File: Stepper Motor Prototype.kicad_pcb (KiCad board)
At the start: 2 copper layers, 37 parts, among them J1 USB_B_Micro, J2 Screw_Terminal_01x02, J3 Screw_Terminal_01x04, Q1 STD20NF06L, Q2 STD20NF06L, Q3 STD20NF06L, Q4 STD20NF06L, Q5 STD20NF06L, Q6 STD20NF06L, Q7 STD20NF06L, Q8 STD20NF06L, U1 FT232RL, U2 ESP8266EX, U3 LM2595SX-3.3_NOPB, U4 MSP430G2553IPW28, U5 LM2595SX-5.0_NOPB, U6 S25FL512SAGMFIG11, U7 DRV8711

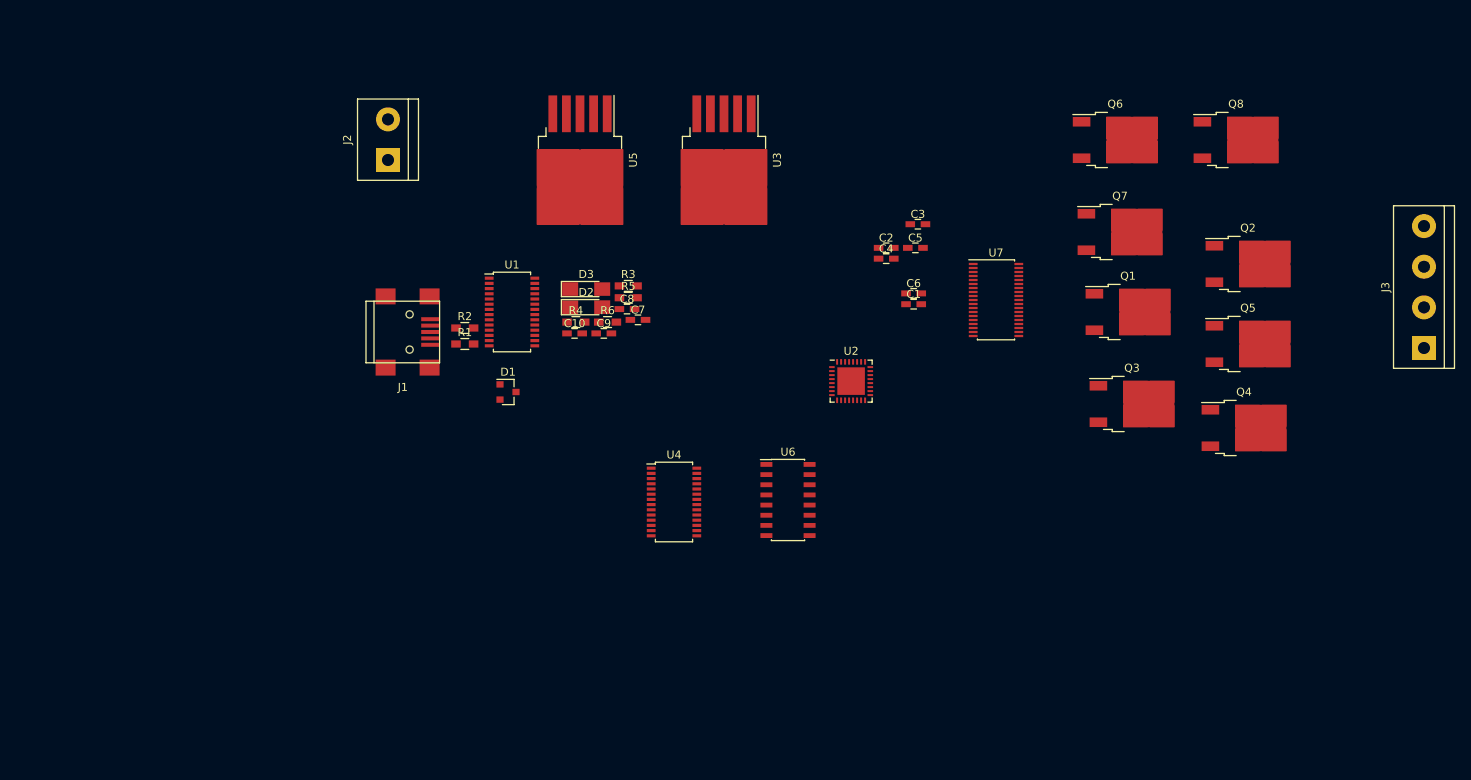
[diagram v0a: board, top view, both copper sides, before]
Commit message: committing before ripping whole board up.  Board will now only contain power seciton and 1 stepper driver
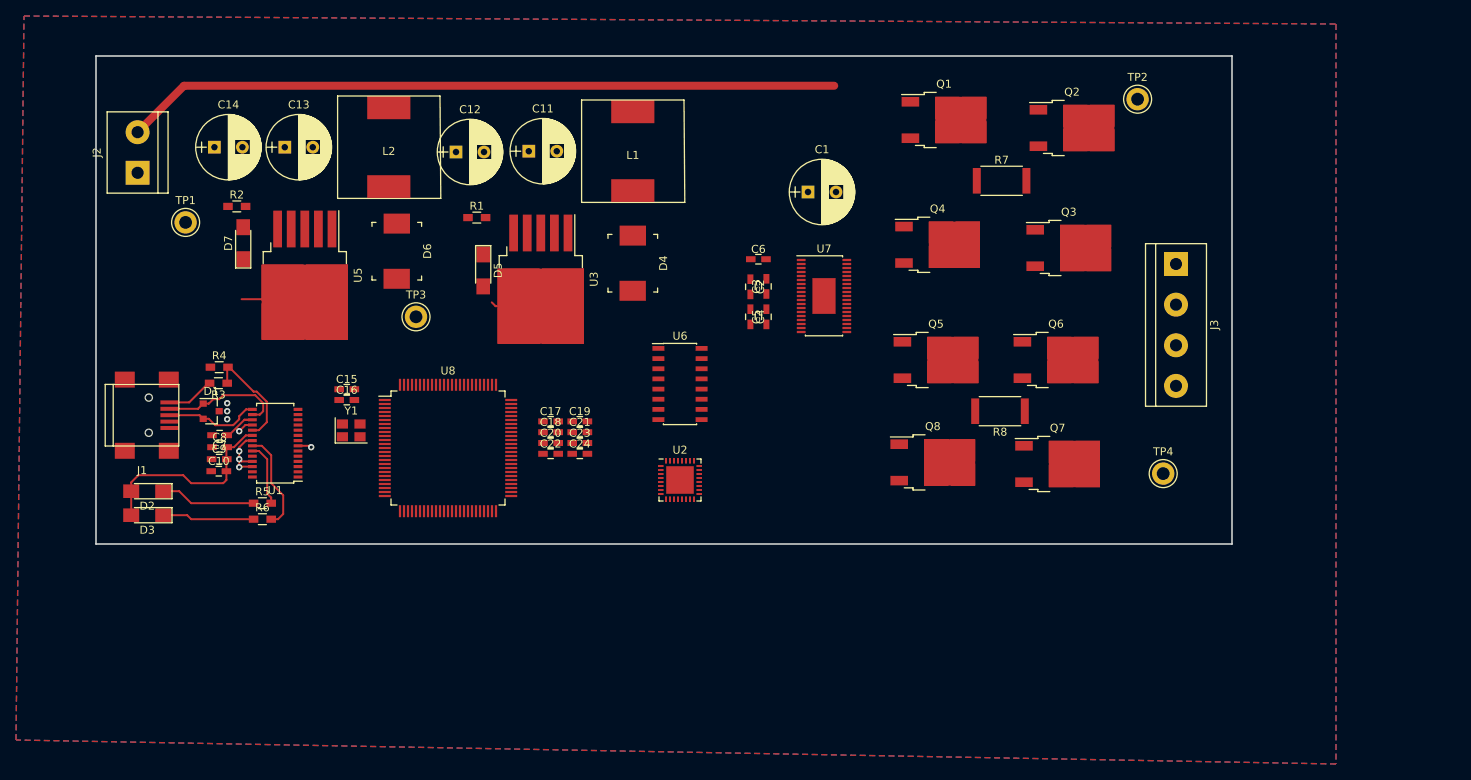
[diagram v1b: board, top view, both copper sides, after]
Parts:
- removed U4: MSP430G2553IPW28, Housings_SSOP:TSSOP-28_4.4x9.7mm_Pitch0.65mm
- added C11: 120uF, Capacitors_THT:CP_Radial_D8.0mm_P3.50mm, F.Cu at (124.1, 68.9)
- added C12: 150uF, Capacitors_THT:CP_Radial_D8.0mm_P3.50mm, F.Cu at (115.0, 69.0)
- added C13: 120uF, Capacitors_THT:CP_Radial_D8.0mm_P3.50mm, F.Cu at (93.6, 68.4)
- added C14: 150uF, Capacitors_THT:CP_Radial_D8.0mm_P3.50mm, F.Cu at (84.8, 68.4)
- added C15: C, Capacitors_SMD:C_0603_HandSoldering, F.Cu at (101.3, 98.7)
- added C16: C, Capacitors_SMD:C_0603_HandSoldering, F.Cu at (101.3, 100.0)
- added C17: 0.1uF, Capacitors_SMD:C_0603_HandSoldering, F.Cu at (126.8, 102.7)
- added C18: 0.1uF, Capacitors_SMD:C_0603_HandSoldering, F.Cu at (126.8, 104.0)
- added C19: 0.1uF, Capacitors_SMD:C_0603_HandSoldering, F.Cu at (130.5, 102.7)
- added C20: 0.1uF, Capacitors_SMD:C_0603_HandSoldering, F.Cu at (126.8, 105.4)
- added C21: 0.1uF, Capacitors_SMD:C_0603_HandSoldering, F.Cu at (130.5, 104.0)
- added C22: 0.1uF, Capacitors_SMD:C_0603_HandSoldering, F.Cu at (126.8, 106.7)
- added C23: 0.1uF, Capacitors_SMD:C_0603_HandSoldering, F.Cu at (130.5, 105.4)
- added C24: 0.1uF, Capacitors_SMD:C_0603_HandSoldering, F.Cu at (130.5, 106.7)
- added D4: D_Schottky, digikey-footprints:DO-214AB, F.Cu at (137.1, 82.9)
- added D5: LED, LEDs:LED_1206_HandSoldering, F.Cu at (118.4, 83.8)
- added D6: D_Schottky, digikey-footprints:DO-214AB, F.Cu at (107.6, 81.4)
- added D7: LED, LEDs:LED_1206_HandSoldering, F.Cu at (88.4, 80.4)
- added L1: 100uH, my_inductors:Wurth_SMD_Inductor_7447709101, F.Cu at (137.1, 68.9)
- added L2: L, my_inductors:Wurth_SMD_Inductor_7447709101, F.Cu at (106.6, 68.4)
- added R7: 0.05R, Resistors_SMD:R_2512, F.Cu at (183.2, 72.6)
- added R8: 0.05R, Resistors_SMD:R_2512, F.Cu at (183.0, 101.4)
- added TP1: TestPoint, Measurement_Points:Test_Point_Keystone_5010-5014_Multipurpose, F.Cu at (81.2, 77.8)
- added TP2: TestPoint, Measurement_Points:Test_Point_Keystone_5010-5014_Multipurpose, F.Cu at (200.2, 62.4)
- added TP3: TestPoint, Measurement_Points:Test_Point_Keystone_5010-5014_Multipurpose, F.Cu at (110.0, 89.6)
- added TP4: TestPoint, Measurement_Points:Test_Point_Keystone_5010-5014_Multipurpose, F.Cu at (203.4, 109.2)
- added U8: STM32F407VGTx, Housings_QFP:LQFP-100_14x14mm_Pitch0.5mm, F.Cu at (114.0, 106.0)
- added Y1: Crystal_GND24, Crystals:Crystal_SMD_SeikoEpson_TSX3225-4pin_3.2x2.5mm, F.Cu at (101.9, 103.8)
- C1: footprint Capacitors_SMD:C_0603_HandSoldering -> Capacitors_THT:CP_Radial_D8.0mm_P3.50mm
- D2: value LED -> TX_LED
- D3: value LED -> RX_LED
- R1, R2: value 68R -> 330R
- U7: footprint Housings_SSOP:TSSOP-38_4.4x9.7mm_Pitch0.5mm -> rca_switch_through_hole:TSSOP-38-1_PowerPad_4.4x9.7mm_Pitch0.5mm
- moved D3 61.7 mm to (76.4, 114.4), turned to 180 degrees
- moved D2 59.5 mm to (76.4, 111.4), turned to 180 degrees
- moved Q8 55.3 mm to (174.6, 107.8)
- moved C7 54.2 mm to (85.5, 104.4), turned to 180 degrees
- moved C8 53.8 mm to (85.5, 105.9)
- moved R3 52.7 mm to (85.3, 97.9), turned to 180 degrees
- moved R5 52.5 mm to (90.8, 112.9)
- moved C9 50.6 mm to (85.4, 107.4)
- moved R6 49.7 mm to (90.8, 114.9)
- moved C10 47.7 mm to (85.3, 108.9)
- moved R4 44.9 mm to (85.4, 95.9)
- moved Q4 44.6 mm to (175.2, 80.6)
- moved Q5 39.1 mm to (175.0, 95.0)
- moved U5 37.3 mm to (96.1, 84.4)
- moved D1 37.2 mm to (84.4, 101.4)
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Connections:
- J1 pad 4: Net-(J1-Pad4) -> (no net)
- Q1 pad 2: Net-(Q1-Pad2) -> +24V
- Q1 pad 3: Net-(Q1-Pad3) -> Net-(J3-Pad1)
- Q2 pad 2: Net-(Q2-Pad2) -> Net-(J3-Pad1)
- Q3 pad 2: Net-(Q3-Pad2) -> Net-(J3-Pad2)
- Q3 pad 3: Net-(Q3-Pad3) -> Net-(Q2-Pad3)
- Q4 pad 2: Net-(Q4-Pad2) -> +24V
- Q4 pad 3: Net-(Q4-Pad3) -> Net-(J3-Pad2)
- Q5 pad 2: Net-(Q5-Pad2) -> +24V
- Q5 pad 3: Net-(Q5-Pad3) -> Net-(J3-Pad3)
- Q6 pad 2: Net-(Q6-Pad2) -> Net-(J3-Pad3)
- Q6 pad 3: Net-(Q6-Pad3) -> Net-(J3-Pad4)
- Q7 pad 3: Net-(Q7-Pad3) -> Net-(J3-Pad4)
- Q8 pad 2: Net-(Q8-Pad2) -> +24V
- Q8 pad 3: Net-(Q8-Pad3) -> Net-(Q7-Pad2)
- R1 pad 1: Net-(R1-Pad1) -> Net-(D5-Pad2)
- R1 pad 2: Net-(D1-Pad2) -> +3V3
- R2 pad 1: Net-(R2-Pad1) -> Net-(D7-Pad2)
- R2 pad 2: Net-(D1-Pad1) -> +5V
- U1 pad 1: Net-(U1-Pad1) -> (no net)
- U1 pad 10: Net-(U1-Pad10) -> (no net)
- U1 pad 11: Net-(U1-Pad11) -> (no net)
- U1 pad 12: Net-(U1-Pad12) -> (no net)
- U1 pad 13: Net-(U1-Pad13) -> (no net)
- U1 pad 14: Net-(U1-Pad14) -> (no net)
- U1 pad 15: Net-(R1-Pad1) -> Net-(D1-Pad2)
- U1 pad 16: Net-(R2-Pad1) -> Net-(D1-Pad1)
- U1 pad 2: Net-(U1-Pad2) -> (no net)
- U1 pad 26: Net-(U1-Pad26) -> GND
- U1 pad 27: Net-(U1-Pad27) -> (no net)
- U1 pad 28: Net-(U1-Pad28) -> (no net)
- U1 pad 3: Net-(U1-Pad3) -> (no net)
- U1 pad 5: Net-(U1-Pad5) -> (no net)
- U1 pad 6: Net-(U1-Pad6) -> (no net)
- U1 pad 9: Net-(U1-Pad9) -> (no net)
- U2 pad 1: Net-(U2-Pad1) -> (no net)
- U2 pad 10: Net-(U2-Pad10) -> (no net)
- U2 pad 11: Net-(U2-Pad11) -> (no net)
- U2 pad 12: Net-(U2-Pad12) -> (no net)
- U2 pad 13: Net-(U2-Pad13) -> (no net)
- U2 pad 14: Net-(U2-Pad14) -> (no net)
- U2 pad 15: Net-(U2-Pad15) -> (no net)
- U2 pad 16: Net-(U2-Pad16) -> (no net)
- U2 pad 17: Net-(U2-Pad17) -> (no net)
- U2 pad 18: Net-(U2-Pad18) -> (no net)
- U2 pad 19: Net-(U2-Pad19) -> (no net)
- U2 pad 2: Net-(U2-Pad2) -> (no net)
- U2 pad 20: Net-(U2-Pad20) -> (no net)
- U2 pad 21: Net-(U2-Pad21) -> (no net)
- U2 pad 22: Net-(U2-Pad22) -> (no net)
- U2 pad 23: Net-(U2-Pad23) -> (no net)
- U2 pad 24: Net-(U2-Pad24) -> (no net)
- U2 pad 25: Net-(U2-Pad25) -> (no net)
- U2 pad 26: Net-(U2-Pad26) -> (no net)
- U2 pad 27: Net-(U2-Pad27) -> (no net)
- U2 pad 28: Net-(U2-Pad28) -> (no net)
- U2 pad 29: Net-(U2-Pad29) -> (no net)
- U2 pad 3: Net-(U2-Pad3) -> (no net)
- U2 pad 30: Net-(U2-Pad30) -> (no net)
- U2 pad 31: Net-(U2-Pad31) -> (no net)
- U2 pad 32: Net-(U2-Pad32) -> (no net)
- U2 pad 4: Net-(U2-Pad4) -> (no net)
- U2 pad 5: Net-(U2-Pad5) -> (no net)
- U2 pad 6: Net-(U2-Pad6) -> (no net)
- U2 pad 7: Net-(U2-Pad7) -> (no net)
- U2 pad 8: Net-(U2-Pad8) -> (no net)
- U2 pad 9: Net-(U2-Pad9) -> (no net)
- U3 pad 1: +3V3 -> Net-(D4-Pad1)
- U3 pad 4: Net-(U3-Pad4) -> +3V3
- U5 pad 1: +5V -> Net-(D6-Pad1)
- U5 pad 4: Net-(U5-Pad4) -> +5V
- U6 pad 1: Net-(U6-Pad1) -> (no net)
- U6 pad 10: Net-(U6-Pad10) -> (no net)
- U6 pad 11: Net-(U6-Pad11) -> (no net)
- U6 pad 12: Net-(U6-Pad12) -> (no net)
- U6 pad 13: Net-(U6-Pad13) -> (no net)
- U6 pad 14: Net-(U6-Pad14) -> (no net)
- U6 pad 15: Net-(U6-Pad15) -> (no net)
- U6 pad 16: Net-(U6-Pad16) -> (no net)
- U6 pad 2: Net-(U6-Pad2) -> (no net)
- U6 pad 3: Net-(U6-Pad3) -> (no net)
- U6 pad 4: Net-(U6-Pad4) -> (no net)
- U6 pad 5: Net-(U6-Pad5) -> (no net)
- U6 pad 6: Net-(U6-Pad6) -> (no net)
- U6 pad 7: Net-(U6-Pad7) -> (no net)
- U6 pad 8: Net-(U6-Pad8) -> (no net)
- U6 pad 9: Net-(U6-Pad9) -> (no net)
- U7 pad 10: Net-(U7-Pad10) -> (no net)
- U7 pad 11: Net-(U7-Pad11) -> (no net)
- U7 pad 12: Net-(U7-Pad12) -> (no net)
- U7 pad 13: Net-(U7-Pad13) -> (no net)
- U7 pad 14: Net-(U7-Pad14) -> (no net)
- U7 pad 15: Net-(U7-Pad15) -> (no net)
- U7 pad 16: Net-(U7-Pad16) -> (no net)
- U7 pad 17: Net-(U7-Pad17) -> (no net)
- U7 pad 18: Net-(U7-Pad18) -> (no net)
- U7 pad 19: Net-(U7-Pad19) -> (no net)
- U7 pad 20: Net-(U7-Pad20) -> (no net)
- U7 pad 21: Net-(U7-Pad21) -> Net-(J3-Pad4)
- U7 pad 22: Net-(U7-Pad22) -> Net-(Q8-Pad1)
- U7 pad 23: Net-(U7-Pad23) -> Net-(Q7-Pad1)
- U7 pad 24: Net-(U7-Pad24) -> GND
- U7 pad 25: Net-(U7-Pad25) -> Net-(J3-Pad4)
- U7 pad 26: Net-(U7-Pad26) -> Net-(Q6-Pad1)
- U7 pad 27: Net-(U7-Pad27) -> Net-(Q5-Pad1)
- U7 pad 28: Net-(U7-Pad28) -> Net-(J3-Pad3)
- U7 pad 30: Net-(U7-Pad30) -> Net-(J3-Pad2)
- U7 pad 31: Net-(U7-Pad31) -> Net-(Q4-Pad1)
- U7 pad 32: Net-(U7-Pad32) -> Net-(Q3-Pad1)
- U7 pad 33: Net-(U7-Pad33) -> GND
- U7 pad 34: Net-(U7-Pad34) -> Net-(Q2-Pad3)
- U7 pad 35: Net-(U7-Pad35) -> Net-(Q2-Pad1)
- U7 pad 36: Net-(U7-Pad36) -> Net-(Q1-Pad1)
- U7 pad 37: Net-(U7-Pad37) -> Net-(J3-Pad1)
- U7 pad 8: Net-(U7-Pad8) -> (no net)
- U7 pad 9: Net-(U7-Pad9) -> (no net)
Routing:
- net +24V: track 0.00 -> 89.5 mm
- net GND: track 0.00 -> 29.8 mm, vias 0 -> 8
- net +5V: track 0.00 -> 24.9 mm
- net Net-(D1-Pad1): track 0.00 -> 15.3 mm
- net Net-(R3-Pad1): track 0.00 -> 13.5 mm
- net Net-(R6-Pad2): track 0.00 -> 12.6 mm
- net Net-(D2-Pad1): track 0.00 -> 11.9 mm
- net Net-(D1-Pad2): track 0.00 -> 11.9 mm
- net Net-(D3-Pad1): track 0.00 -> 11.5 mm
- net Net-(R5-Pad2): track 0.00 -> 7.98 mm
- net Net-(J1-Pad1): track 0.00 -> 5.99 mm
- net Net-(C7-Pad1): track 0.00 -> 4.35 mm
- added copper zone on B.Cu, net GND
- added copper zone on F.Cu, net GND
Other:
- board outline added: 142 x 61 mm
- net class Power added: clearance 0.2, trace_width 1, via_dia 1.5, via_drill 1.1
